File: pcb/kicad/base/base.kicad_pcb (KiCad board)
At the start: 2 copper layers, 38 parts, among them P1 Test_MUX, P2 J-Link SWD, P3 Vbatt-V_test, P4 Vbatt_I-test, P5 CHIP_EN, U1 SAMB11G18A, U2 XBee-PRO_900HP, Y1 32.768kHz, Y2 26MHz

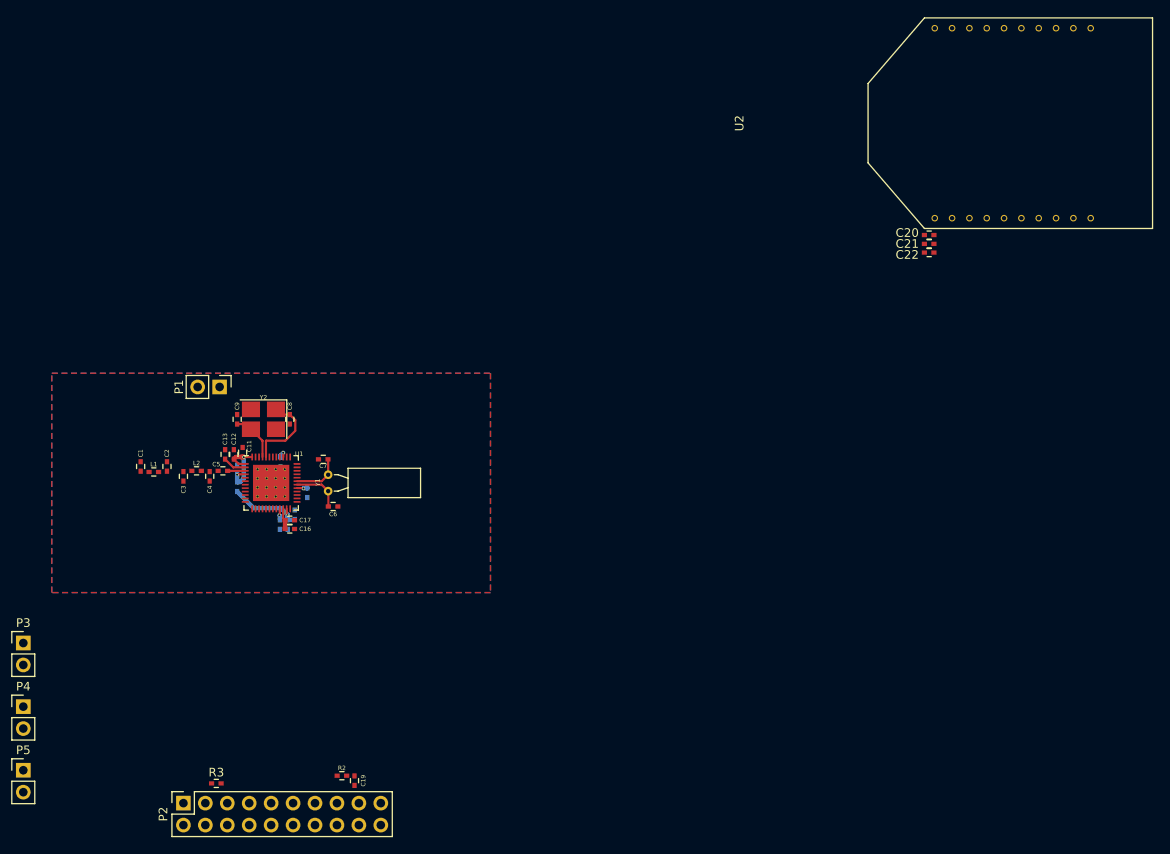
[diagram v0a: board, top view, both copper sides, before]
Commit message: Cleanup crystals and 2.4GHz RF end
UART pins dedicated for 900MHz XBee operations may need to be moved,
keeping the 2.4GHz and 900MHz signals as far apart as possible. SMA jack
substituted for 2.4GHz antenna for first prototype; expecting to measure
input impedance.
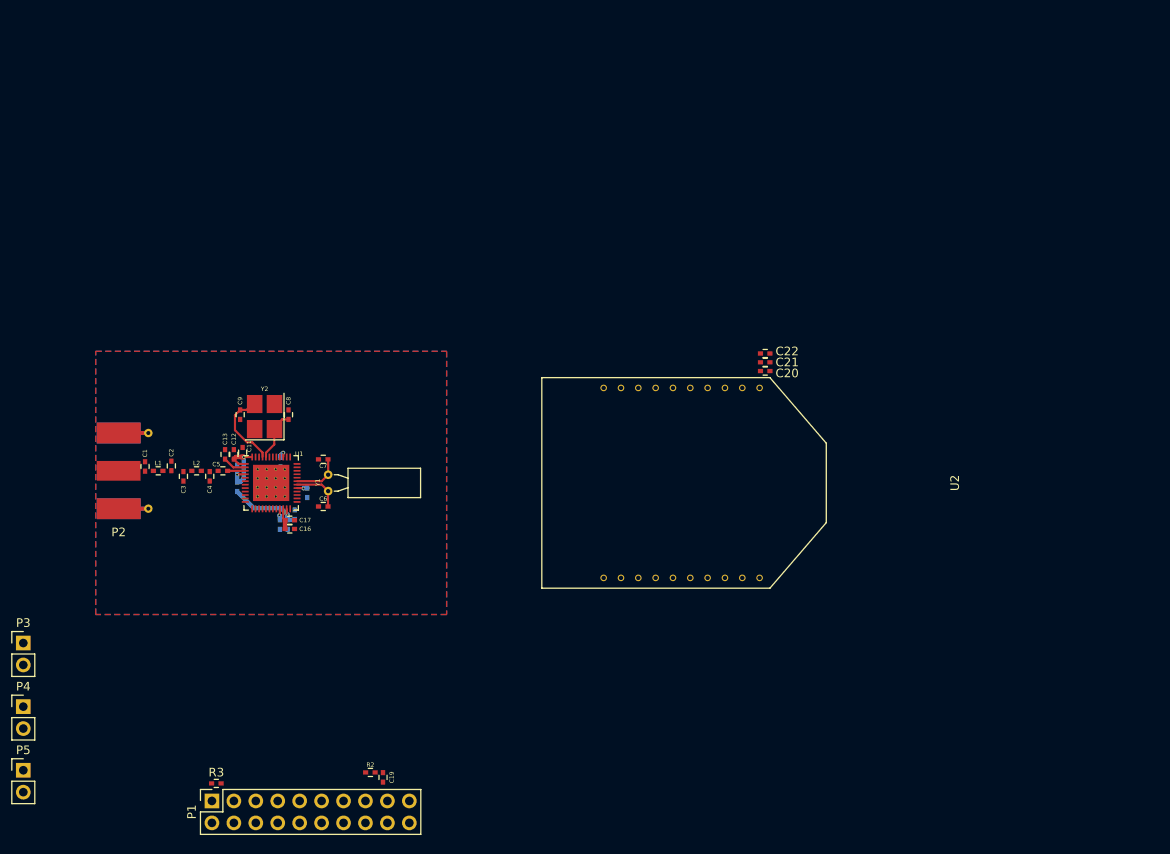
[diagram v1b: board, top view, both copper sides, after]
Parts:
- P1: value Test_MUX -> J-Link SWD; footprint Socket_Strips:Socket_Strip_Straight_1x02_Pitch2.54mm -> Socket_Strips:Socket_Strip_Straight_2x10_Pitch2.54mm
- P2: value J-Link SWD -> CONN_01X02; footprint Socket_Strips:Socket_Strip_Straight_2x10_Pitch2.54mm -> Misc:Molex_SMA_Jack_Edge_Mount
- moved U2 48.6 mm to (202.8, 88.9), turned to 270 degrees
- moved P1 48.0 mm to (141.7, 125.7), turned to 90 degrees
- moved P2 38.9 mm to (132.7, 87.5), turned to 0 degrees
- moved C20 24.7 mm to (205.8, 75.9), turned to 0 degrees
- moved C21 23.4 mm to (205.8, 74.9), turned to 0 degrees
- moved C22 22.3 mm to (205.8, 73.9), turned to 0 degrees
- moved C19 3.32 mm to (161.5, 123.0)
- moved R2 3.32 mm to (160.1, 122.4)
- moved C6 1.14 mm to (154.6, 91.6), turned to 180 degrees
- moved C9 0.64 mm to (145.0, 81.0), turned to 270 degrees
- moved C8 0.55 mm to (150.6, 81.0), turned to 90 degrees
- moved L1 0.52 mm to (135.5, 87.5)
- moved C2 0.51 mm to (137.0, 86.9)
- moved C1 0.51 mm to (134.0, 87.0)
- moved Y2 0.34 mm to (147.8, 81.2), turned to 90 degrees
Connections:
- P1 pad 1: Net-(P1-Pad1) -> /+3.3V
- P2 pad 1: /+3.3V -> /SIG_2.4G
- P2 pad 2: Net-(P2-Pad2) -> GND
- P5 pad 1: Net-(P2-Pad15) -> Net-(P1-Pad15)
- R2 pad 1: Net-(P2-Pad15) -> Net-(P1-Pad15)
- U1 pad 26: Net-(P2-Pad15) -> Net-(P1-Pad15)
- U1 pad 46: Net-(P1-Pad1) -> Net-(U1-Pad46)
- U1 pad 47: Net-(P1-Pad2) -> Net-(U1-Pad47)
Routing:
- net Net-(C8-Pad1): track 9.73 -> 5.87 mm
- net Net-(C9-Pad1): track 5.62 -> 9.39 mm

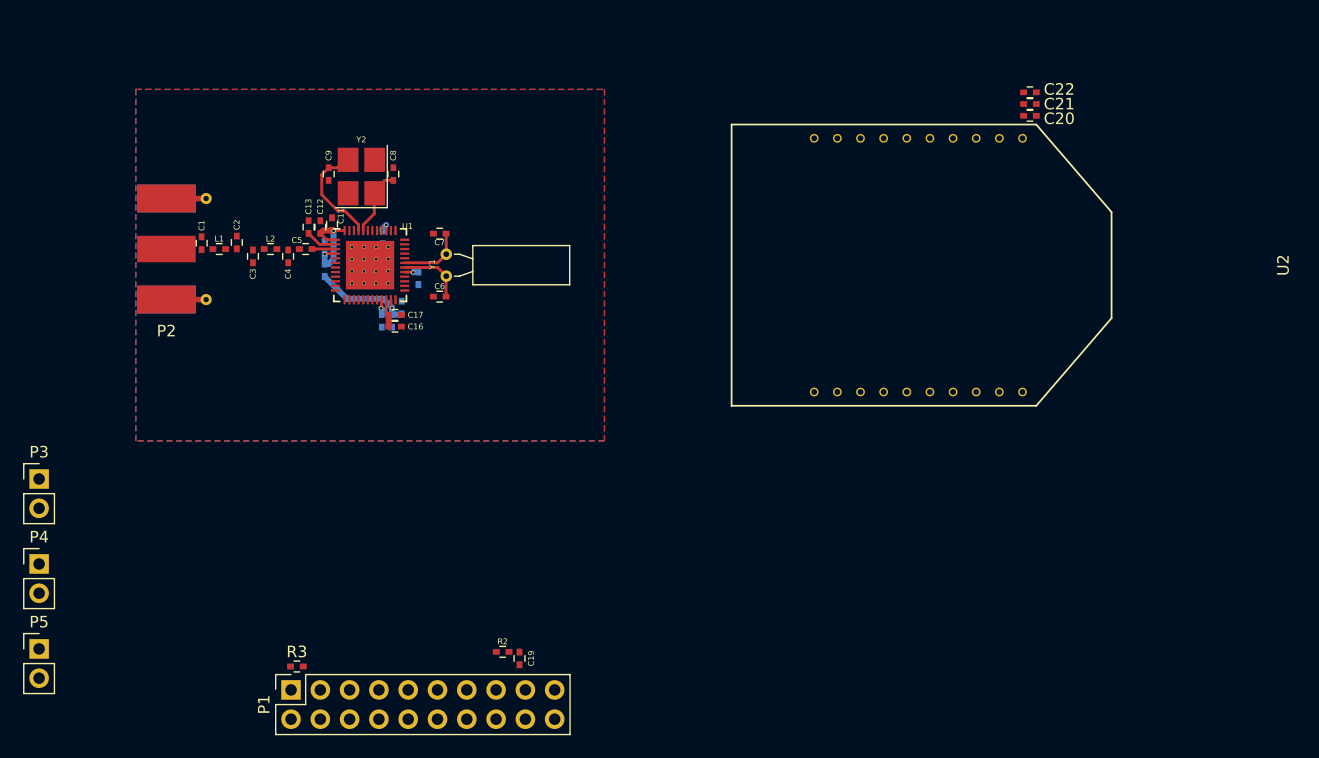
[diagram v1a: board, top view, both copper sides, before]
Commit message: Add more progress to crystal and XBee routing
Crystal has been moved to create a cleaner top layer for better signal
pathing. Daughterboard concept starting to be realized by adding vias
of pin header dimensions. Power routing still needs to be redone, and
and holes for ground header pins need to be placed.
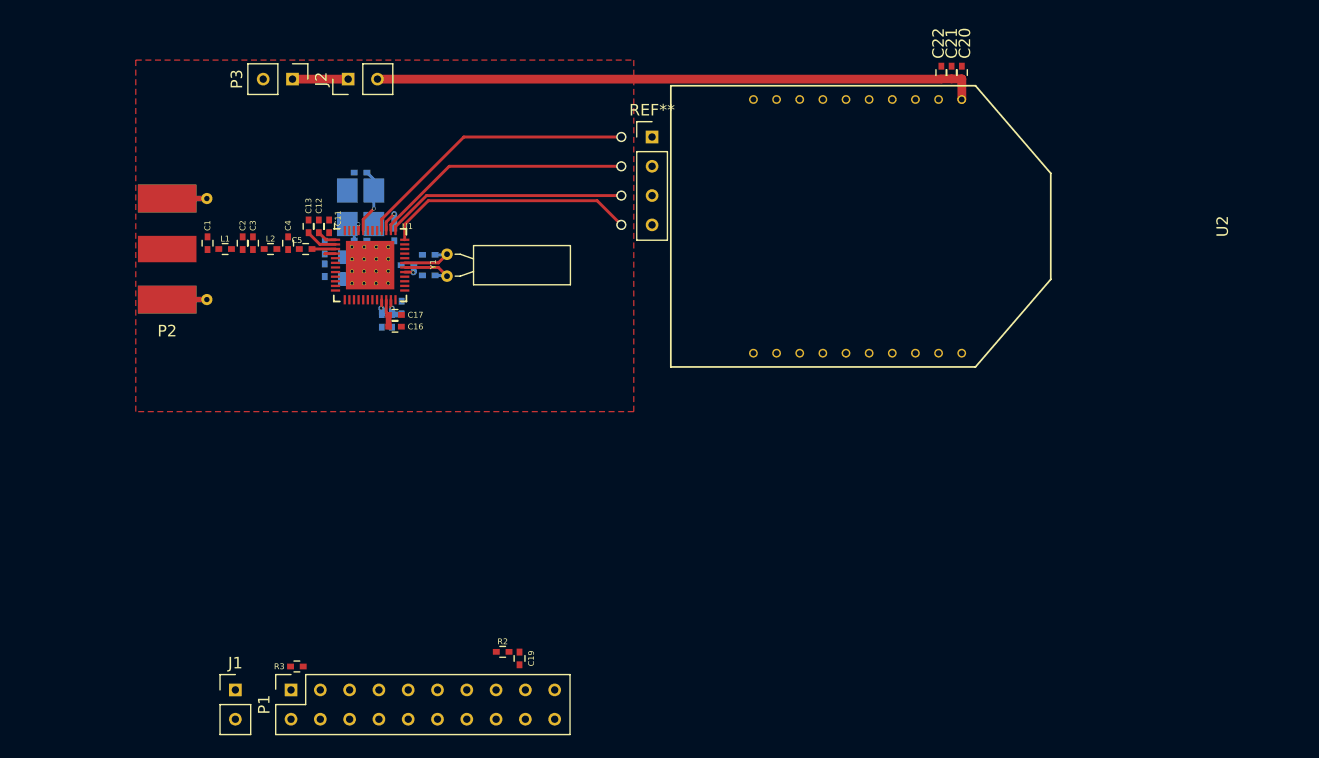
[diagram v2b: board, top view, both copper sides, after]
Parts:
- removed P4: Vbatt_I-test, Socket_Strips:Socket_Strip_Straight_1x02_Pitch2.54mm
- removed P5: CHIP_EN, Socket_Strips:Socket_Strip_Straight_1x02_Pitch2.54mm
- added FB1: BLM03AG121SN1, Capacitors_SMD:C_0603_HandSoldering, B.Cu at (146.2, 89.2)
- added J1: CHIP_EN, Socket_Strips:Socket_Strip_Straight_1x02_Pitch2.54mm, F.Cu at (136.9, 125.7)
- added J2: Vbatt_I-test, Socket_Strips:Socket_Strip_Straight_1x02_Pitch2.54mm, F.Cu at (146.7, 72.8)
- added REF**: Socket_Strip_Straight_1x04_Pitch2.54mm, Socket_Strips:Socket_Strip_Straight_1x04_Pitch2.54mm, F.Cu at (173.0, 77.8)
- C6, C7, C8, C9, Y2: moved to B.Cu
- P3: value Vbatt-V_test -> Power Source
- moved P3 41.0 mm to (141.9, 72.8), turned to 270 degrees
- moved C22 7.87 mm to (198.1, 72.2), turned to 90 degrees
- moved C21 7.32 mm to (199.0, 72.2), turned to 90 degrees
- moved C20 6.99 mm to (199.9, 72.2), turned to 90 degrees
- moved C9 6.39 mm to (147.8, 86.8), turned to 0 degrees
- moved U2 6.25 mm to (197.5, 85.5)
- moved C8 2.84 mm to (147.8, 80.9), turned to 180 degrees
- moved Y2 2.67 mm to (147.8, 83.9), turned to 270 degrees
- moved C6 2.07 mm to (153.7, 89.8)
- moved C7 2.07 mm to (153.7, 88.0)
- moved C18 1.49 mm to (151.8, 88.9), turned to 180 degrees
- moved C3 1.14 mm to (138.4, 87.0), turned to 90 degrees
- moved C4 1.14 mm to (141.5, 87.0), turned to 90 degrees
- moved C15 1.05 mm to (150.7, 86.2)
- moved C2 0.51 mm to (137.5, 87.0)
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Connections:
- C15 pad 1: Net-(C15-Pad1) -> /+3.3V
- C16 pad 1: Net-(C15-Pad1) -> /+3.3V
- C17 pad 1: Net-(C15-Pad1) -> /+3.3V
- P3 pad 1: Net-(C15-Pad1) -> Net-(J2-Pad1)
- U1 pad 22: Net-(C15-Pad1) -> /+3.3V
- U1 pad 24: /GPIO_MS1 -> GND
- U1 pad 25: /GPIO_MS2 -> GND
- U1 pad 27: /GPIO_MS3 -> GND
- U1 pad 28: /GPIO_MS4 -> GND
- U1 pad 36: /LP_GPIO_14 -> /UART_RTS
- U1 pad 37: /LP_GPIO_15 -> /UART_CTS
- U1 pad 38: /LP_GPIO_16 -> /UART_RX
- U1 pad 39: Net-(C15-Pad1) -> /+3.3V
- U1 pad 40: /LP_GPIO_17 -> /UART_TX
- U2 pad 12: /LP_GPIO_4 -> /UART_CTS
- U2 pad 16: /LP_GPIO_5 -> /UART_RTS
- U2 pad 2: /LP_GPIO_2 -> /UART_RX
- U2 pad 3: /LP_GPIO_3 -> /UART_TX
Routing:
- net /+3.3V: track 0.00 -> 57.9 mm, vias 0 -> 1
- net /UART_TX: track 0.00 -> 24.7 mm, vias 0 -> 1
- net /UART_RX: track 0.00 -> 22.6 mm, vias 0 -> 1
- net /UART_RTS: track 0.00 -> 21.8 mm, vias 0 -> 1
- net /UART_CTS: track 0.00 -> 21.0 mm, vias 0 -> 1
- net Net-(C14-Pad1): track 9.18 -> 2.16 mm
- net Net-(C10-Pad1): track 9.16 -> 2.66 mm, vias 2 -> 0
- net Net-(C9-Pad1): track 9.39 -> 3.21 mm, vias 0 -> 1
- net Net-(J2-Pad1): track 0.00 -> 4.70 mm
- net Net-(C15-Pad1): track 3.58 -> 0.00 mm, vias 1 -> 0
- net Net-(C7-Pad1): track 5.71 -> 5.04 mm
- net Net-(C6-Pad1): track 5.73 -> 5.10 mm
- net Net-(C8-Pad1): track 5.87 -> 5.66 mm, vias 0 -> 1
- removed copper zone on B.Cu, net GND
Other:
- net class Default: via_dia 0.3556 -> 0.3048
- rule via_min_size: 0.3556 -> 0.254

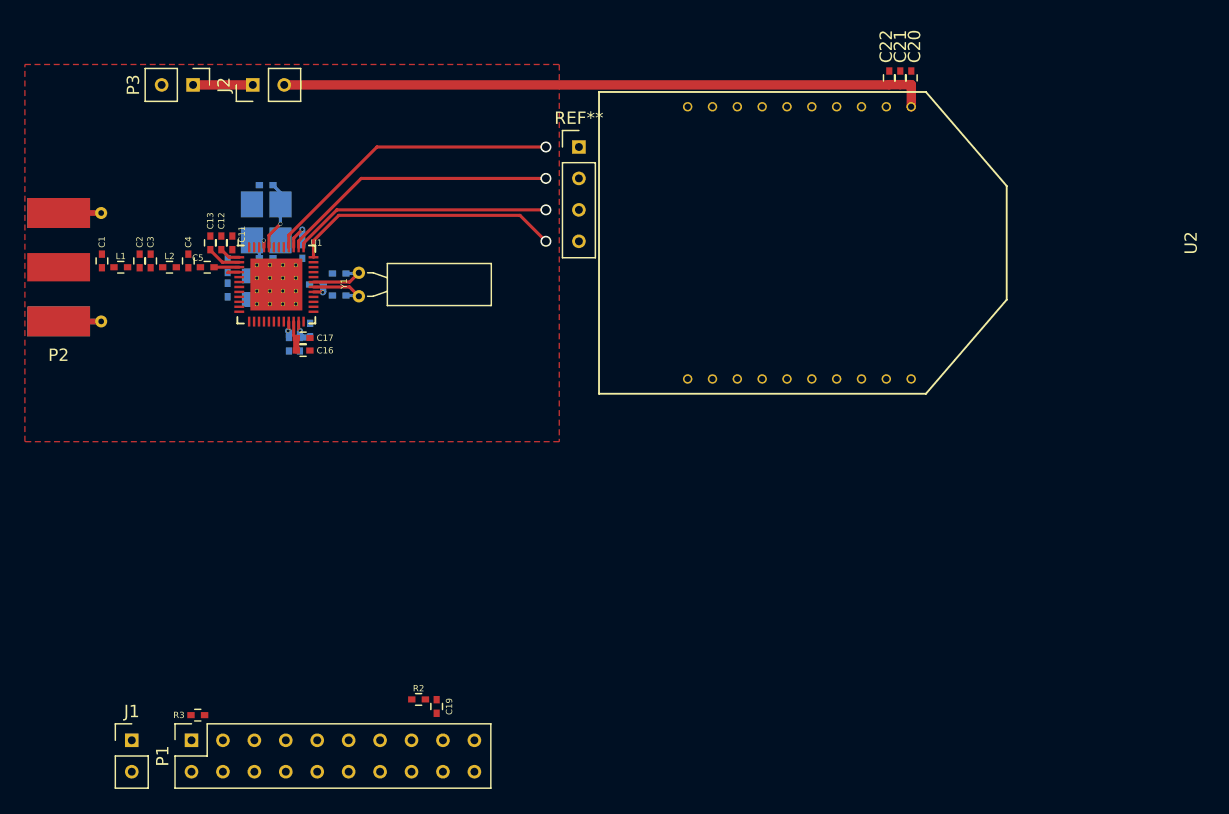
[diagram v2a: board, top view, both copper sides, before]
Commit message: Add header pins into design
Header pins have been implemented into design, keeping in mind the
prototyping goal of a daugther-mother board design. For first revision,
the plan has changed to become a single board. For further revisions,
assuming the daugtherboard portion works properly, it will be sheared
and mounted on header pins, positioned meticulously with convenient
vias. Power is almost completely routed. Ground vias to be completed.
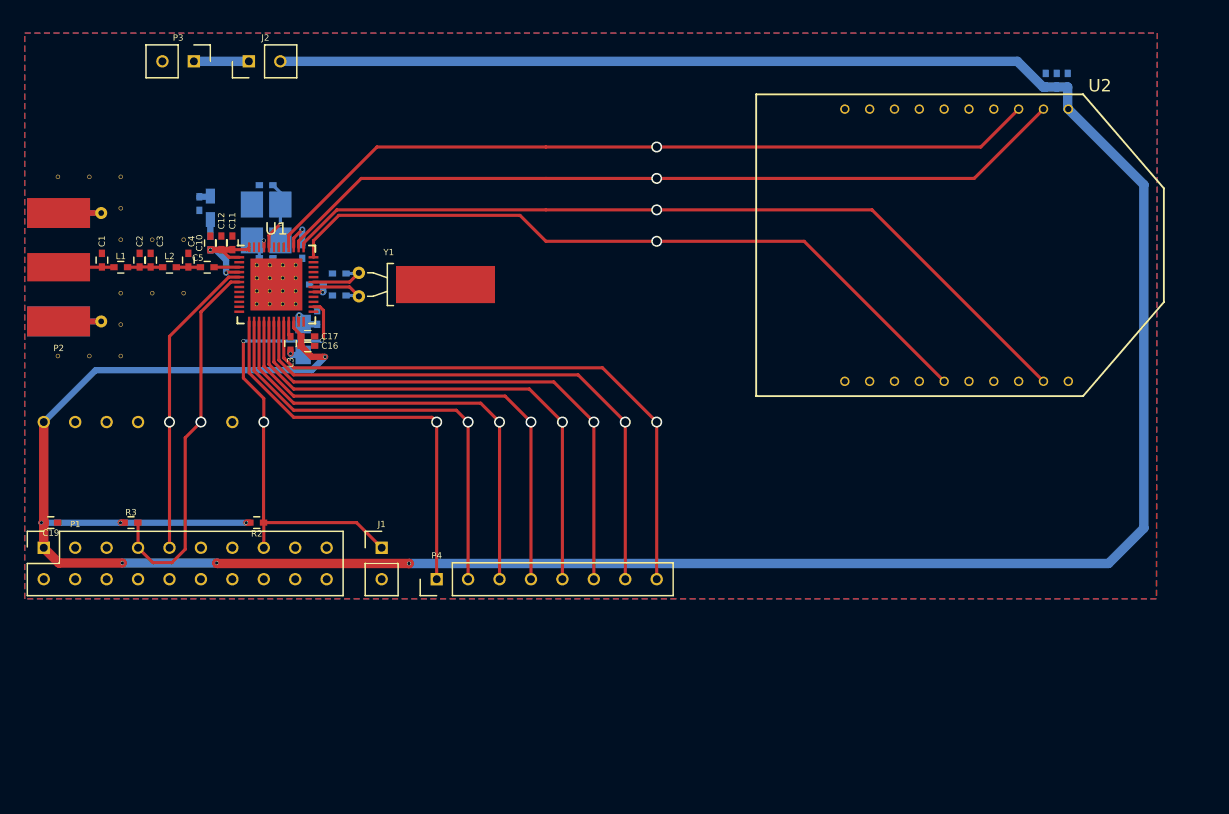
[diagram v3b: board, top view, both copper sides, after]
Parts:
- removed the REF** at (173.0, 77.8)
- added P4: CONN_01X08, Misc:Socket_Strip_Straight_1x08_Pitch2.54mm_Drill0.64mm, F.Cu at (161.5, 112.7)
- added REF**: Via_Stitch_Dia1.00mm_Drill0.64mm, Misc:Via_Stitch_Dia1.00mm_Drill0.64mm, F.Cu at (145.0, 100.0)
- added REF**: Via_Stitch_Dia0.356mm_Drill0.254mm, Misc:Via_Stitch_Dia0.356mm_Drill0.254mm, F.Cu at (136.0, 92.1)
- added REF**: Via_Stitch_Dia0.356mm_Drill0.254mm, Misc:Via_Stitch_Dia0.356mm_Drill0.254mm, F.Cu at (136.0, 94.7)
- added REF**: Via_Stitch_Dia0.356mm_Drill0.254mm, Misc:Via_Stitch_Dia0.356mm_Drill0.254mm, F.Cu at (133.5, 94.7)
- added REF**: Via_Stitch_Dia0.356mm_Drill0.254mm, Misc:Via_Stitch_Dia0.356mm_Drill0.254mm, F.Cu at (130.9, 94.7)
- added REF**: Via_Stitch_Dia0.356mm_Drill0.254mm, Misc:Via_Stitch_Dia0.356mm_Drill0.254mm, F.Cu at (133.5, 80.2)
- added REF**: Via_Stitch_Dia0.356mm_Drill0.254mm, Misc:Via_Stitch_Dia0.356mm_Drill0.254mm, F.Cu at (130.9, 80.2)
- added REF**: Via_Stitch_Dia0.356mm_Drill0.254mm, Misc:Via_Stitch_Dia0.356mm_Drill0.254mm, F.Cu at (138.6, 85.3)
- added REF**: Via_Stitch_Dia0.356mm_Drill0.254mm, Misc:Via_Stitch_Dia0.356mm_Drill0.254mm, F.Cu at (141.1, 85.3)
- added REF**: Via_Stitch_Dia0.356mm_Drill0.254mm, Misc:Via_Stitch_Dia0.356mm_Drill0.254mm, F.Cu at (138.6, 89.6)
- added REF**: Via_Stitch_Dia0.356mm_Drill0.254mm, Misc:Via_Stitch_Dia0.356mm_Drill0.254mm, F.Cu at (141.1, 89.6)
- added REF**: Via_Stitch_Dia1.00mm_Drill0.64mm, Misc:Via_Stitch_Dia1.00mm_Drill0.64mm, F.Cu at (129.8, 100.0)
- added REF**: Via_Stitch_Dia1.00mm_Drill0.64mm, Misc:Via_Stitch_Dia1.00mm_Drill0.64mm, F.Cu at (137.4, 100.0)
- added REF**: Via_Stitch_Dia1.00mm_Drill0.64mm, Misc:Via_Stitch_Dia1.00mm_Drill0.64mm, F.Cu at (134.9, 100.0)
- added REF**: Via_Stitch_Dia1.00mm_Drill0.64mm, Misc:Via_Stitch_Dia1.00mm_Drill0.64mm, F.Cu at (132.3, 100.0)
- added REF**: Via_Stitch_Dia0.356mm_Drill0.254mm, Misc:Via_Stitch_Dia0.356mm_Drill0.254mm, F.Cu at (136.0, 85.3)
- added REF**: Via_Stitch_Dia0.356mm_Drill0.254mm, Misc:Via_Stitch_Dia0.356mm_Drill0.254mm, F.Cu at (136.0, 89.6)
- added REF**: Via_Stitch_Dia0.356mm_Drill0.254mm, Misc:Via_Stitch_Dia0.356mm_Drill0.254mm, F.Cu at (136.0, 82.7)
- added REF**: Via_Stitch_Dia0.356mm_Drill0.254mm, Misc:Via_Stitch_Dia0.356mm_Drill0.254mm, F.Cu at (136.0, 80.2)
- C10, L3: moved to F.Cu
- C13, C20, C21, C22: moved to B.Cu
- C14: value 0.1uF -> 4.7uF 6.3V
- C16: value 2.2uF -> 2.2uF 6.3V
- J1, J2, P3: footprint Socket_Strips:Socket_Strip_Straight_1x02_Pitch2.54mm -> Misc:Socket_Strip_Straight_1x02_Pitch2.54mm_Drill0.64mm
- L4: footprint Capacitors_SMD:C_0402 -> Capacitors_SMD:C_0805_HandSoldering
- P1: footprint Socket_Strips:Socket_Strip_Straight_2x10_Pitch2.54mm -> Misc:Socket_Strip_Straight_2x10_Pitch2.54mm_Drill0.64mm
- P2: value CONN_01X02 -> SMA
- U1: value SAMB11G18A -> SAMB11G18A-edit; footprint Housings:QFN-48-1EP_6x6mm_Pitch0.4mm -> QFN-48-1EP_6x6mm_Pitch0.4mm
- Y1: footprint Crystals:Crystal_C38-LF_d3.0mm_l8.0mm_Horizontal -> Crystals:Crystal_C38-LF_d3.0mm_l8.0mm_Horizontal_1EP_style1
- moved C19 34.5 mm to (130.4, 108.1), turned to 0 degrees
- moved J1 25.5 mm to (157.1, 110.2)
- moved P1 19.6 mm to (129.8, 110.2)
- moved R2 19.4 mm to (147.0, 108.1), turned to 180 degrees
- moved R3 16.5 mm to (136.8, 108.1)
- moved U2 12.7 mm to (210.2, 85.7)
- moved C20 12.6 mm to (212.5, 72.4)
- moved C21 12.6 mm to (211.6, 72.4)
- moved C22 12.6 mm to (210.8, 72.4)
- moved FB1 7.08 mm to (143.3, 82.7)
- moved R1 4.05 mm to (143.3, 85.5), turned to 270 degrees
- moved C13 3.30 mm to (142.4, 82.4), turned to 270 degrees
- moved C10 2.30 mm to (143.3, 85.5)
- moved J2 1.93 mm to (146.4, 70.9)
- moved P3 1.91 mm to (141.9, 70.9)
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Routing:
- net /+3.3V: track 57.9 -> 253.3 mm, vias 1 -> 8
- net /LP_GPIO_13: track 0.00 -> 47.9 mm, vias 0 -> 1
- net /UART_CTS: track 21.0 -> 67.0 mm
- net /LP_GPIO_12: track 0.00 -> 45.9 mm, vias 0 -> 1
- net /LP_GPIO_11: track 0.00 -> 43.8 mm, vias 0 -> 1
- net /UART_RX: track 22.6 -> 65.1 mm
- net /LP_GPIO_10: track 0.00 -> 41.8 mm, vias 0 -> 1
- net /LP_GPIO_9: track 0.00 -> 39.8 mm, vias 0 -> 1
- net /UART_TX: track 24.7 -> 64.2 mm
- net /LP_GPIO_8: track 0.00 -> 37.7 mm, vias 0 -> 1
- net Net-(J1-Pad1): track 0.00 -> 37.6 mm, vias 0 -> 3
- net /UART_RTS: track 21.8 -> 58.7 mm
- net /LP_GPIO_7: track 0.00 -> 35.7 mm, vias 0 -> 1
- net /LP_GPIO_6: track 0.00 -> 33.6 mm, vias 0 -> 1
- net /SWDIO: track 0.00 -> 30.6 mm, vias 0 -> 1
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- added copper zone on B.Cu, net GND
